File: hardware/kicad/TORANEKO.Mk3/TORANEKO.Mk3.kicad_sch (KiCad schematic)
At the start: 93 parts, among them IC1 MP6551GQB-P, IC2 MP6551GQB-P, IC3 NCR321PASX, IC4 NCR321PASX, IC5 AS5047P-ATSM, IC6 STM32F411CEU6TR, IC7 AS5047P-ATSM, IC8 NCR321PASX, IC9 NCR321PASX, J1 Conn_01x02_Pin, J2 Conn_01x02_Pin, J3 Conn_01x02_Male, J4 Conn_01x02_Pin, J5 Conn_01x02_Pin, J6 Conn_02x03_Odd_Even, Q1 IRLML6402, Q5 IRLML6344, SW1 SW_Push, U1 LSM6DSRXTR, U2 LXDC55FAAA-203, U3 Encord, U4 Encord_B, U5 Encord, U6 Encord_B, Y1 CSTNE10M0G52Z000R0

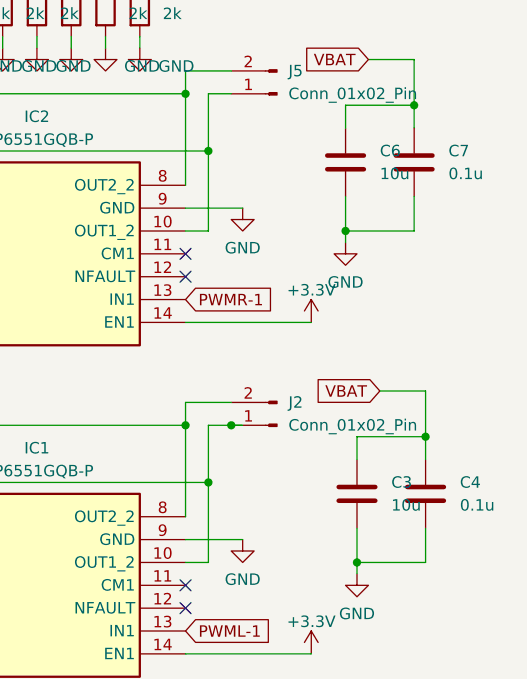
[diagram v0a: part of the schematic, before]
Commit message: C3/C6 (VBAT): 10uF -> 1uF 25V 0402 and add to PCBA BOM
No 0402 10uF part rated >=16V exists, and VBAT is 2S LiPo (8.4V max);
C2 (100uF) remains as bulk capacitance.

Co-Authored-By: Claude Opus 5.5 <noreply@anthropic.com>
Claude-Session: https://claude.ai/code/session_01Cv6KpZe6NLHWQTjQMUz9Sg
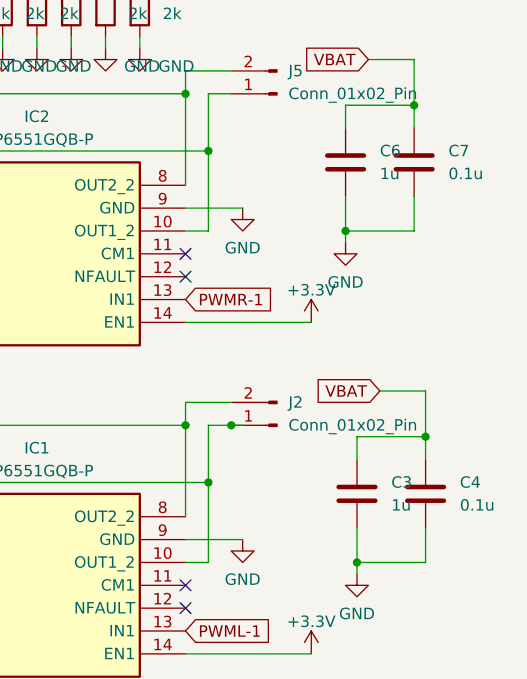
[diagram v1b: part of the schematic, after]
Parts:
- C3, C6: value 10u -> 1u
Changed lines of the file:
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@@
 			)
 		)
-		(property "Value" "10u"
+		(property "Value" "1u"
 			(at 273.05 143.5099 0)
 			(effects
@@
 			)
 		)
-		(property "Value" "10u"
+		(property "Value" "1u"
 			(at 271.78 106.6799 0)
 			(effects

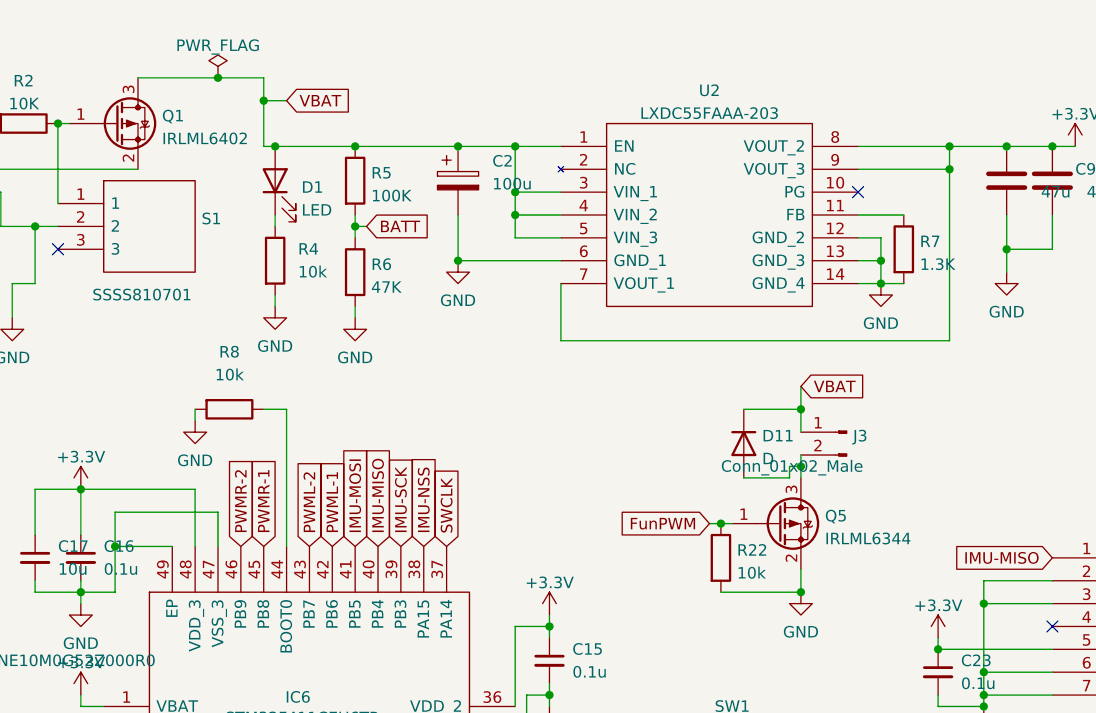
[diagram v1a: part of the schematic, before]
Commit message: Q1/Q5: IRLML6402/6344 -> AO3401A/AO3400A (JLC Basic parts)
Same SOT-23 pinout (1=G, 2=S, 3=D) and +-12V Vgs rating; removes two
Extended parts from the PCBA order.

Co-Authored-By: Claude Opus 5.5 <noreply@anthropic.com>
Claude-Session: https://claude.ai/code/session_01Cv6KpZe6NLHWQTjQMUz9Sg
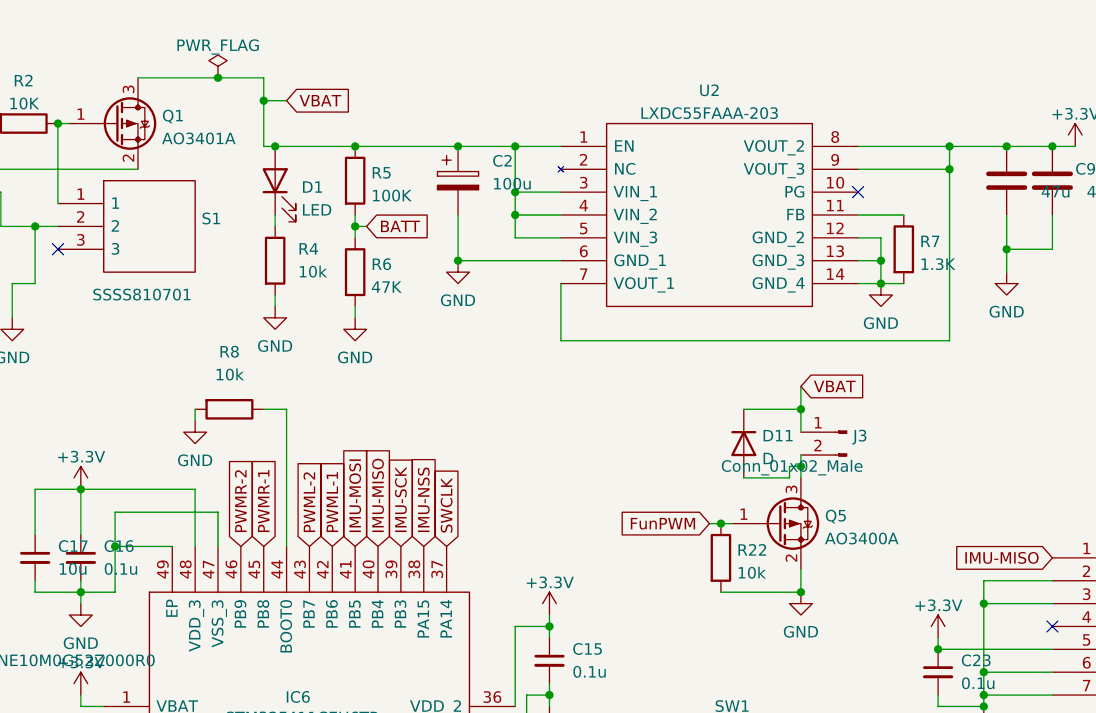
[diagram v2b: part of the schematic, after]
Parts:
- Q1: value IRLML6402 -> AO3401A
- Q5: value IRLML6344 -> AO3400A
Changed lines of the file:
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@@
 			)
 		)
-		(property "Value" "IRLML6402"
+		(property "Value" "AO3401A"
 			(at 52.197 27.1022 0)
 			(effects
@@
 			)
 		)
-		(property "Value" "IRLML6344"
+		(property "Value" "AO3400A"
 			(at 125.857 71.5522 0)
 			(effects

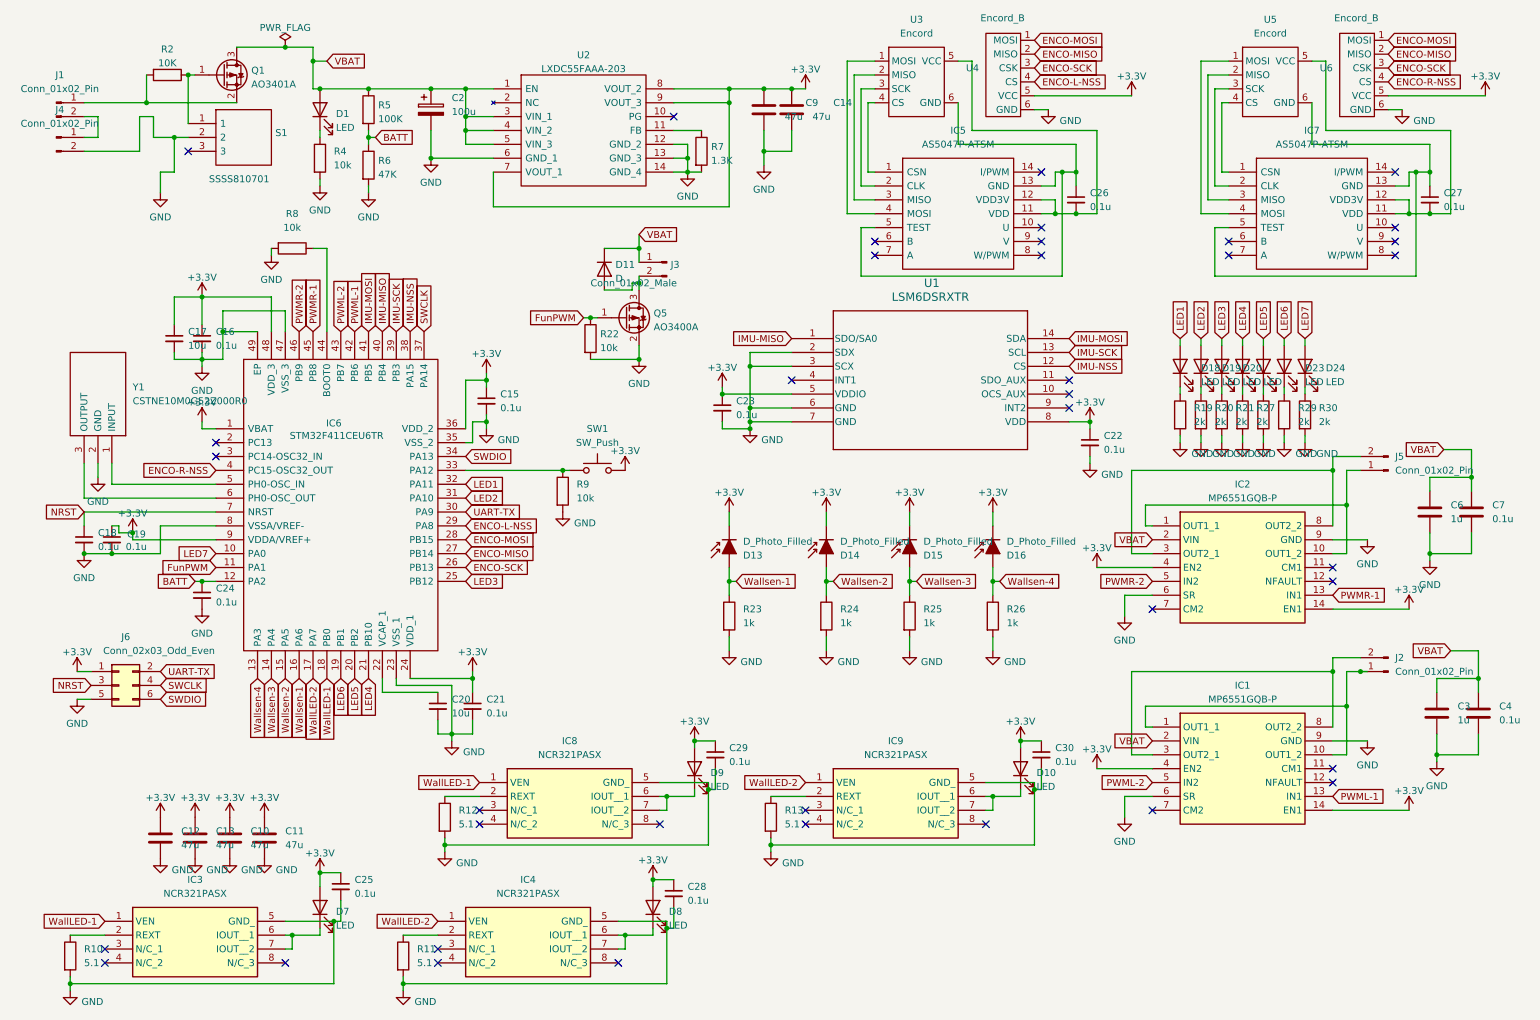
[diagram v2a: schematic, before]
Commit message: C9-C14 (+3.3V): 47uF -> 22uF 0603 (JLC Basic C59461)
Co-Authored-By: Claude Opus 5.5 <noreply@anthropic.com>
Claude-Session: https://claude.ai/code/session_01Cv6KpZe6NLHWQTjQMUz9Sg
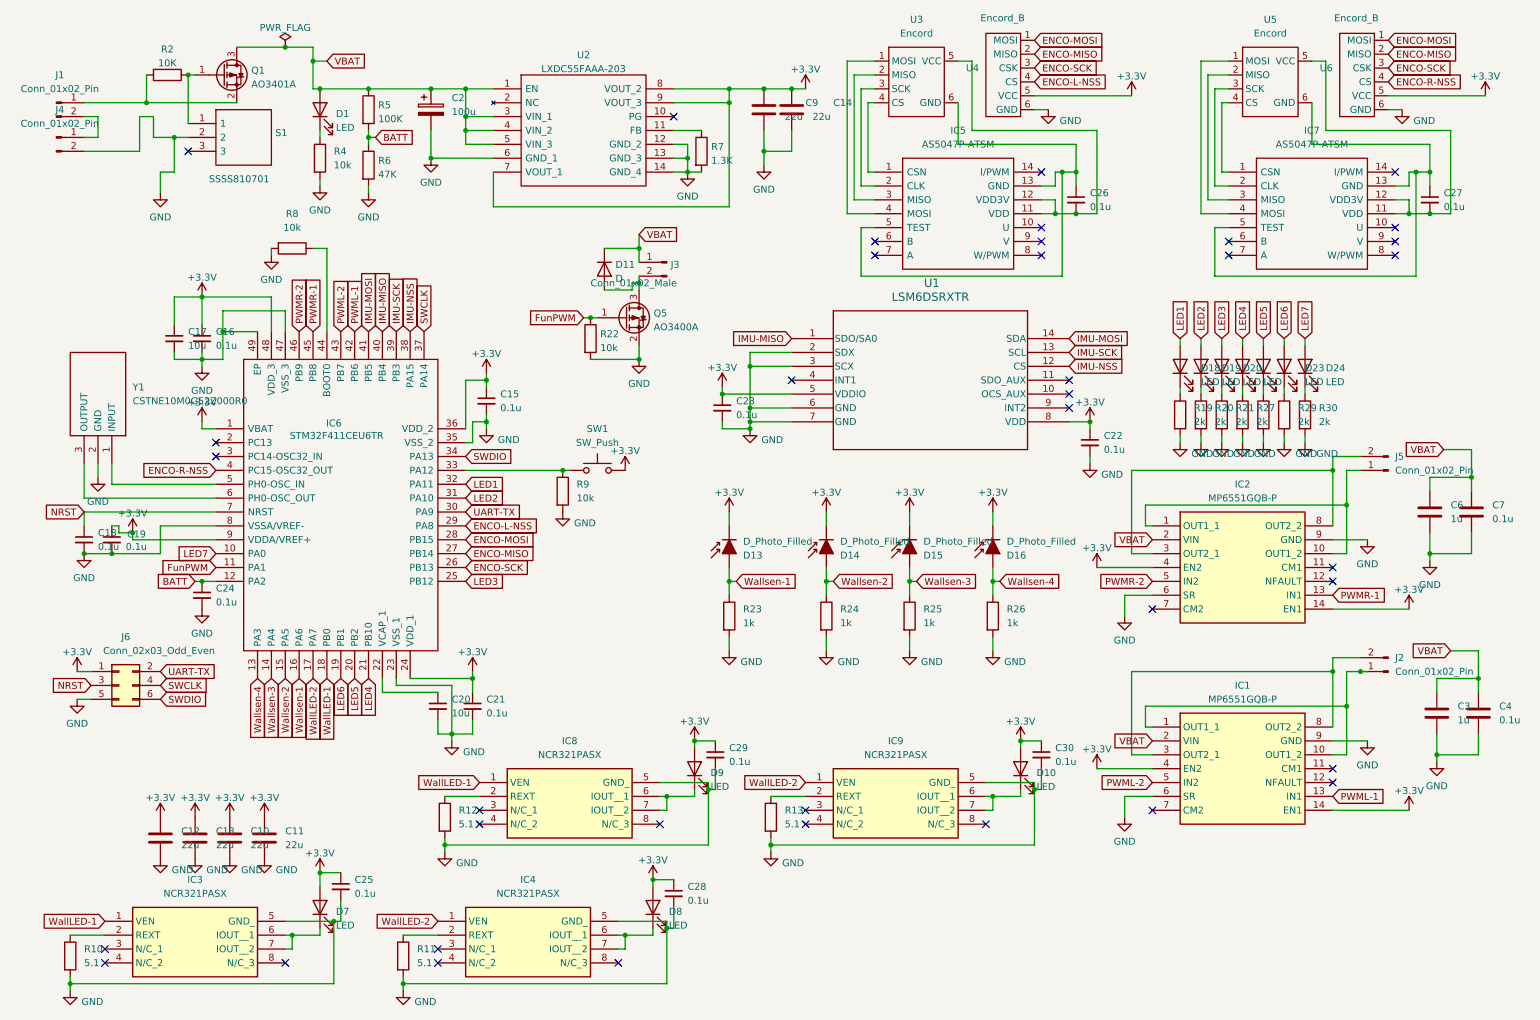
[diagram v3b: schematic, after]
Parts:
- C10, C11, C12, C13, C14, C9: value 47u -> 22u
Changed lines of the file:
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@@
 			)
 		)
-		(property "Value" "47u"
+		(property "Value" "22u"
 			(at 39.37 166.3699 0)
 			(effects
@@
 			)
 		)
-		(property "Value" "47u"
+		(property "Value" "22u"
 			(at 149.86 33.0199 0)
 			(effects
@@
 			)
 		)
-		(property "Value" "47u"
+		(property "Value" "22u"
 			(at 154.94 33.0199 0)
 			(effects
@@
 			)
 		)
-		(property "Value" "47u"
+		(property "Value" "22u"
 			(at 52.07 166.3699 0)
 			(effects
@@
 			)
 		)
-		(property "Value" "47u"
+		(property "Value" "22u"
 			(at 45.72 166.3699 0)
 			(effects
@@
 			)
 		)
-		(property "Value" "47u"
+		(property "Value" "22u"
 			(at 58.42 166.3699 0)
 			(effects

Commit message: Status LEDs: red -> blue (C130724); LED resistors 2k -> 1k
Blue Vf (~2.6V+) leaves only ~0.5V across the resistor from a 3.3V GPIO;
1k gives ~0.5mA instead of ~0.25mA. 1k is already in the BOM, so the
2k line is dropped (17 part types). D1 stays on R4 10k from VBAT.

Co-Authored-By: Claude Opus 5.5 <noreply@anthropic.com>
Claude-Session: https://claude.ai/code/session_01Cv6KpZe6NLHWQTjQMUz9Sg
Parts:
- R19, R20, R21, R27, R28, R29, R30: value 2k -> 1k
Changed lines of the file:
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@@
 			)
 		)
-		(property "Value" "2k"
+		(property "Value" "1k"
 			(at 232.41 88.8999 0)
 			(effects
@@
 			)
 		)
-		(property "Value" "2k"
+		(property "Value" "1k"
 			(at 247.65 88.8999 0)
 			(effects
@@
 			)
 		)
-		(property "Value" "2k"
+		(property "Value" "1k"
 			(at 228.6 88.8999 0)
 			(effects
@@
 			)
 		)
-		(property "Value" "2k"
+		(property "Value" "1k"
 			(at 243.84 88.8999 0)
 			(effects
@@
 			)
 		)
-		(property "Value" "2k"
+		(property "Value" "1k"
 			(at 240.03 88.8999 0)
 			(effects
@@
 			)
 		)
-		(property "Value" "2k"
+		(property "Value" "1k"
 			(at 224.79 88.8999 0)
 			(effects
@@
 			)
 		)
-		(property "Value" "2k"
+		(property "Value" "1k"
 			(at 236.22 88.8999 0)
 			(effects

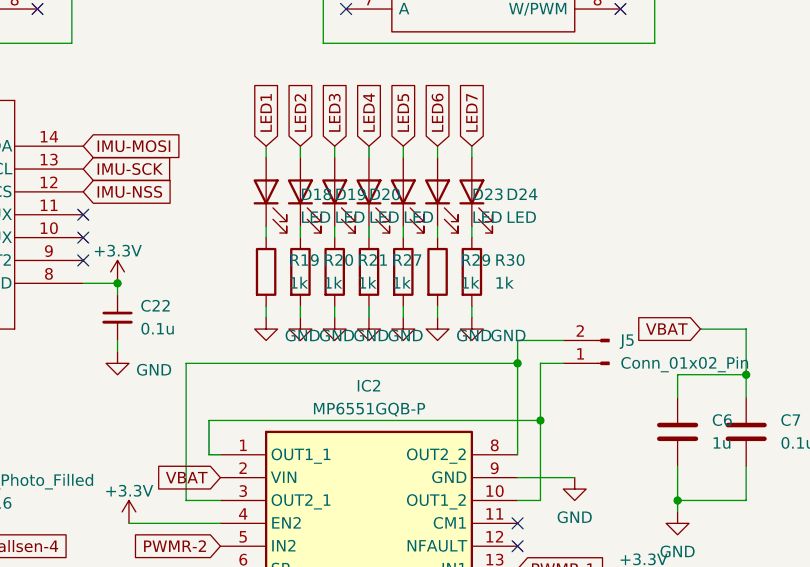
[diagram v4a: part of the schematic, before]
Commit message: LED resistors back to 2k (blue at 1k was too bright); record the order
Blue LEDs (C130724) stay. Panel README notes that the main board was
ordered as a single board with JLCPCB-added rails, 3 boards assembled.

Co-Authored-By: Claude Opus 5.5 <noreply@anthropic.com>
Claude-Session: https://claude.ai/code/session_01Cv6KpZe6NLHWQTjQMUz9Sg
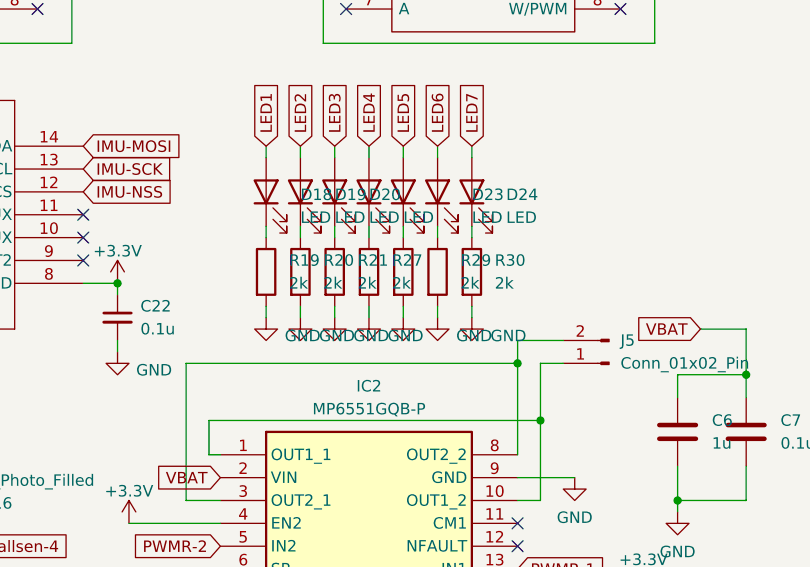
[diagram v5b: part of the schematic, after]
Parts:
- R19, R20, R21, R27, R28, R29, R30: value 1k -> 2k
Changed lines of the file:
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@@
 			)
 		)
-		(property "Value" "1k"
+		(property "Value" "2k"
 			(at 232.41 88.8999 0)
 			(effects
@@
 			)
 		)
-		(property "Value" "1k"
+		(property "Value" "2k"
 			(at 247.65 88.8999 0)
 			(effects
@@
 			)
 		)
-		(property "Value" "1k"
+		(property "Value" "2k"
 			(at 228.6 88.8999 0)
 			(effects
@@
 			)
 		)
-		(property "Value" "1k"
+		(property "Value" "2k"
 			(at 243.84 88.8999 0)
 			(effects
@@
 			)
 		)
-		(property "Value" "1k"
+		(property "Value" "2k"
 			(at 240.03 88.8999 0)
 			(effects
@@
 			)
 		)
-		(property "Value" "1k"
+		(property "Value" "2k"
 			(at 224.79 88.8999 0)
 			(effects
@@
 			)
 		)
-		(property "Value" "1k"
+		(property "Value" "2k"
 			(at 236.22 88.8999 0)
 			(effects
